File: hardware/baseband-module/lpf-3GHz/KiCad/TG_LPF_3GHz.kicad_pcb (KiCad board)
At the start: 2 copper layers, 19 x 19 mm, 15 parts

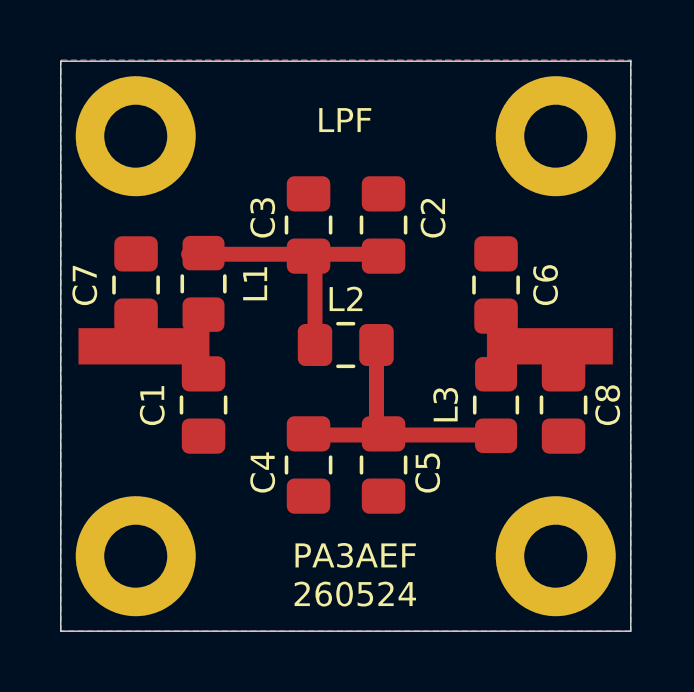
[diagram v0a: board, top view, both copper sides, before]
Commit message: Add positions CSV file for control module components in KiCad
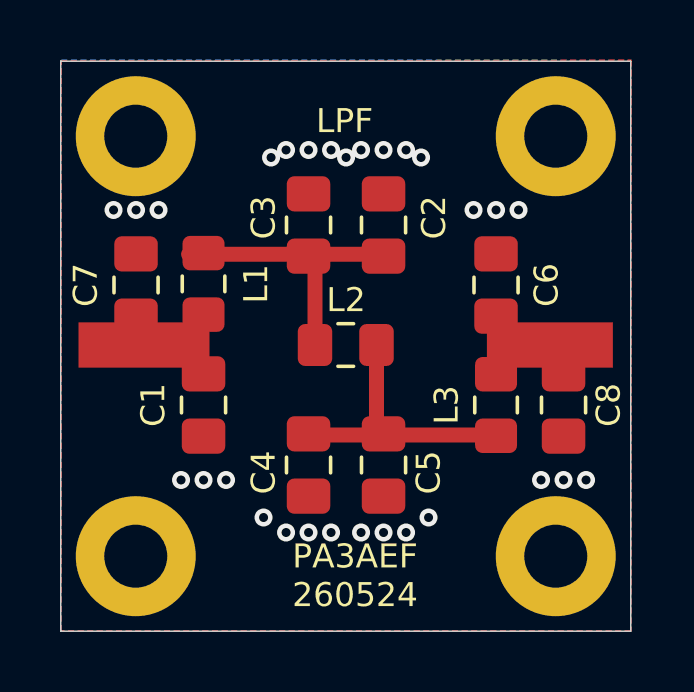
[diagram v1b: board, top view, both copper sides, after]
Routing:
- net GND: vias 0 -> 29
